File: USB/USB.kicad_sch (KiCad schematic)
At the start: 33 parts, among them J1 MISC1, U1 TLV61222

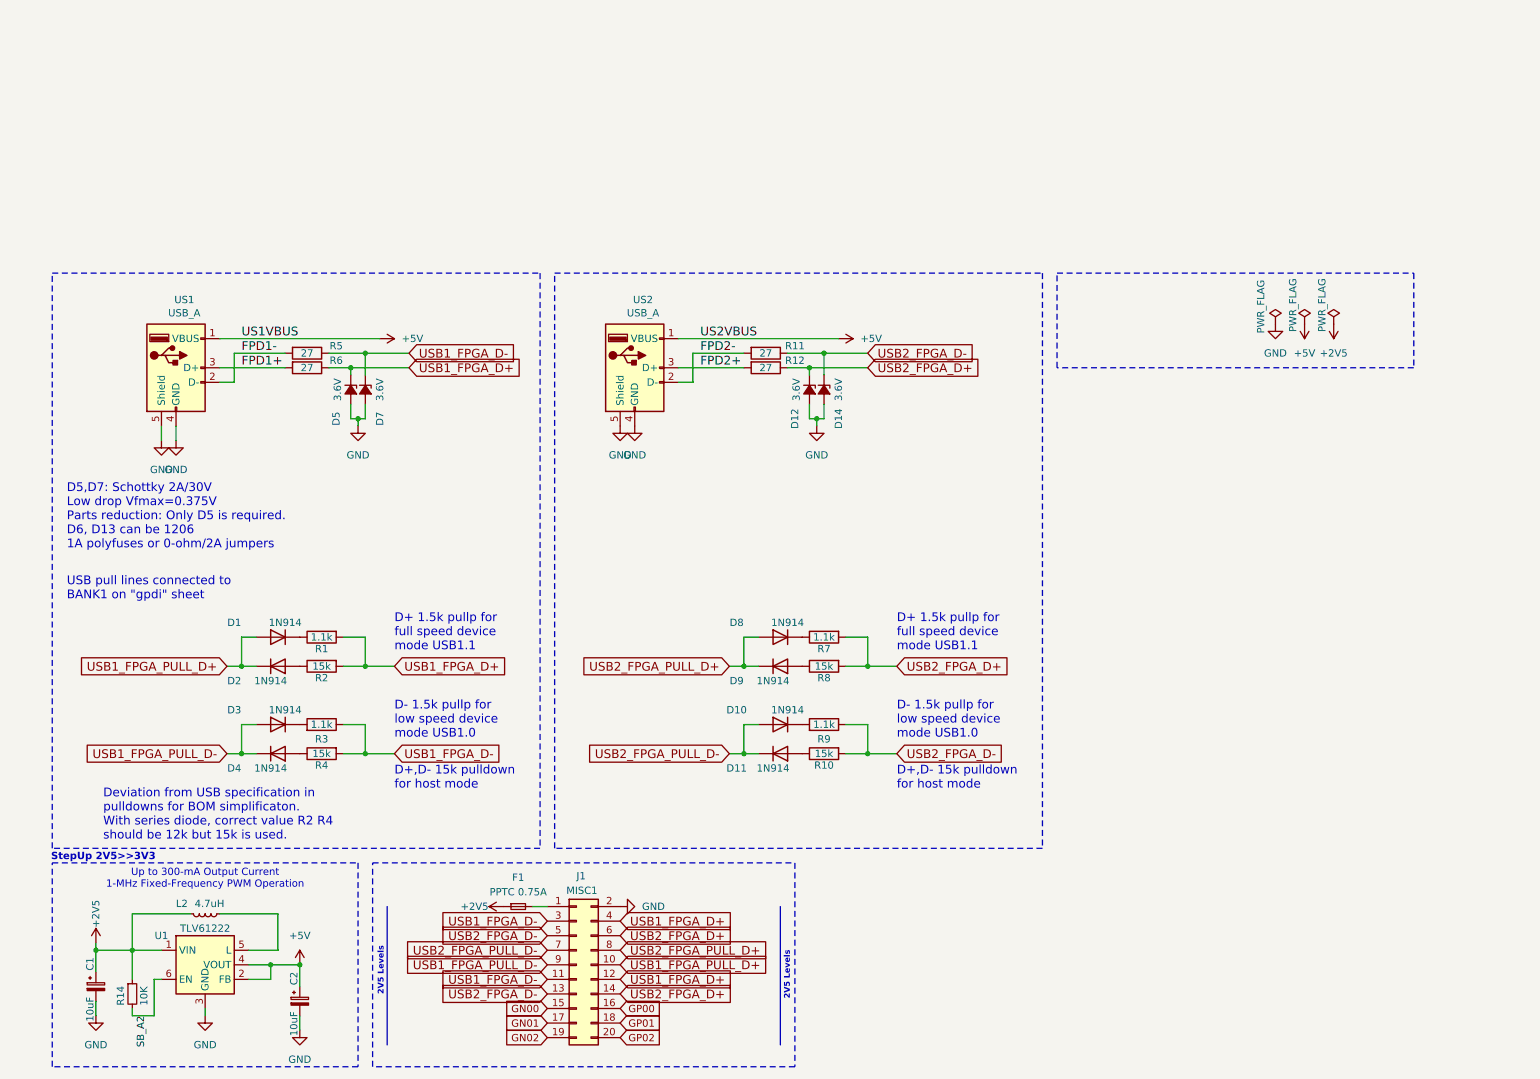
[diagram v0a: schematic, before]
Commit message: Updating USB
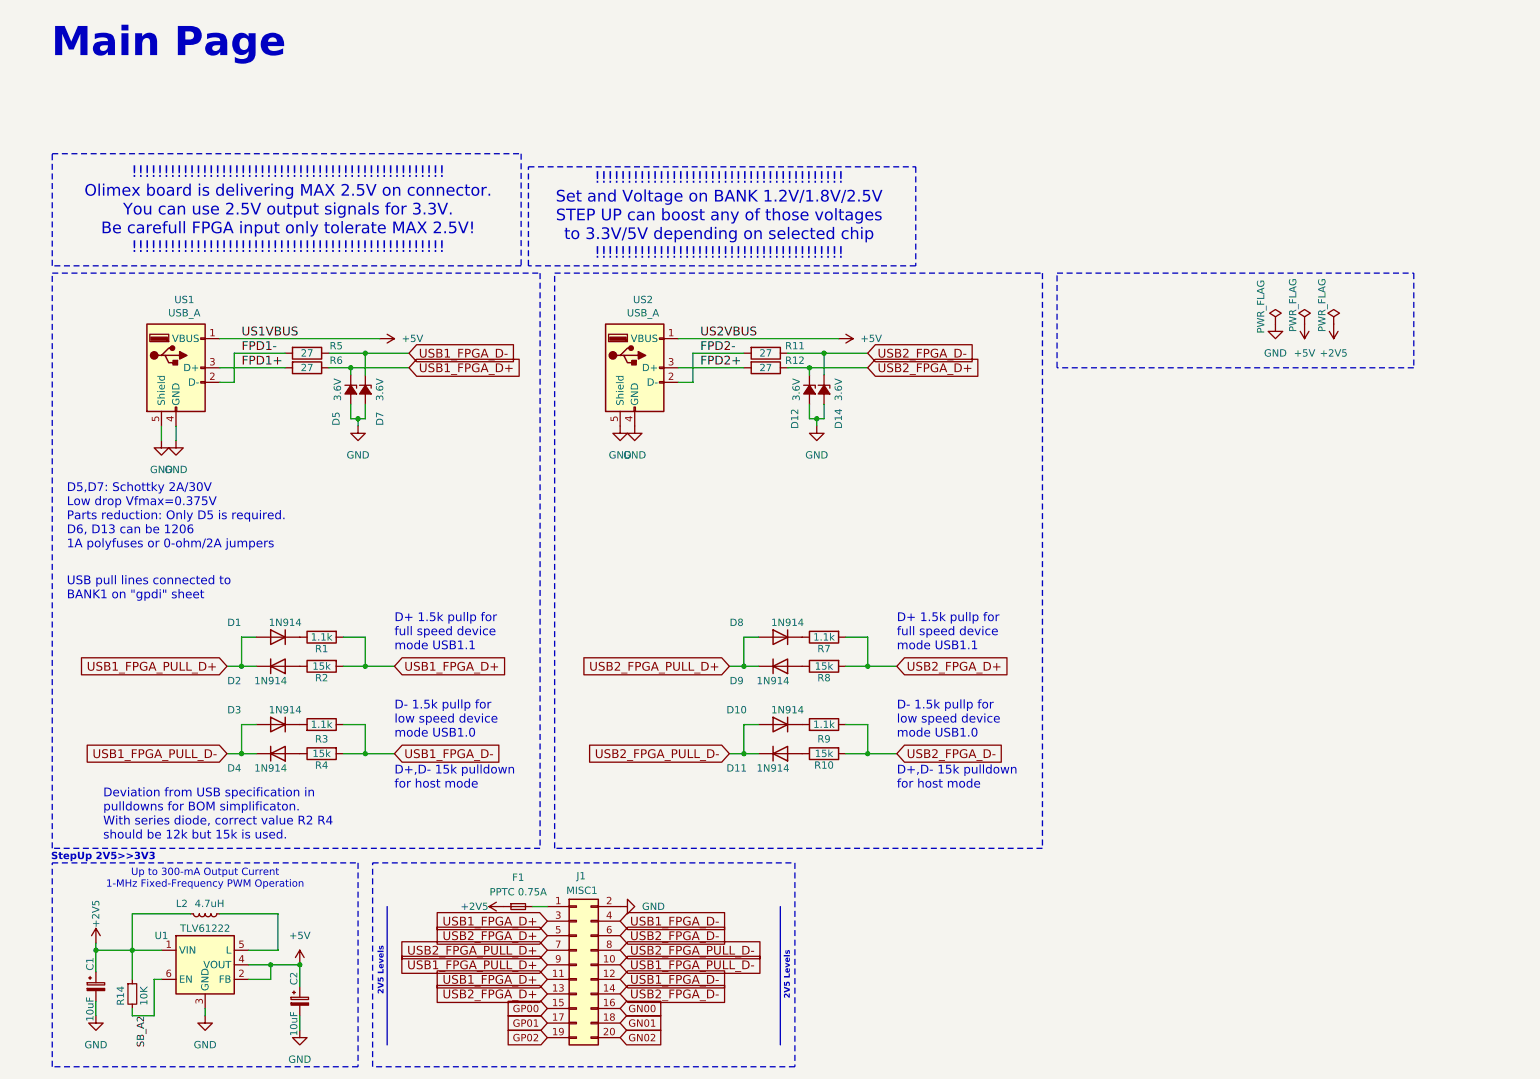
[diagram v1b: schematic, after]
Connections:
- net GN00: now also J1.16 (Pin_16); no longer J1.15 (Pin_15)
- net GN01: now also J1.18 (Pin_18); no longer J1.17 (Pin_17)
- net GN02: now also J1.20 (Pin_20); no longer J1.19 (Pin_19)
- net GP00: now also J1.15 (Pin_15); no longer J1.16 (Pin_16)
- net GP01: now also J1.17 (Pin_17); no longer J1.18 (Pin_18)
- net GP02: now also J1.19 (Pin_19); no longer J1.20 (Pin_20)
- net USB1_FPGA_D+: now also J1.11 (Pin_11), J1.3 (Pin_3); no longer J1.12 (Pin_12), J1.4 (Pin_4)
- net USB1_FPGA_D-: now also J1.12 (Pin_12), J1.4 (Pin_4); no longer J1.11 (Pin_11), J1.3 (Pin_3)
- net USB1_FPGA_PULL_D+: now also J1.9 (Pin_9); no longer J1.10 (Pin_10)
- net USB1_FPGA_PULL_D-: now also J1.10 (Pin_10); no longer J1.9 (Pin_9)
- net USB2_FPGA_D+: now also J1.13 (Pin_13), J1.5 (Pin_5); no longer J1.14 (Pin_14), J1.6 (Pin_6)
- net USB2_FPGA_D-: now also J1.14 (Pin_14), J1.6 (Pin_6); no longer J1.13 (Pin_13), J1.5 (Pin_5)
- net USB2_FPGA_PULL_D+: now also J1.7 (Pin_7); no longer J1.8 (Pin_8)
- net USB2_FPGA_PULL_D-: now also J1.8 (Pin_8); no longer J1.7 (Pin_7)
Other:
- note added: "!!!!!!!!!!!!!!!!!!!!!!!!!!!!!!!!!!!!!!! Set and Voltage on BANK 1.2V/1.8V/2.5V STEP UP can boost any of those voltages to 3.3V/5V depending on selected chip !!!!!!!!!!!!!!!!!!!!!!!!!!!!!!!!!!!!!!!"
- note added: "!!!!!!!!!!!!!!!!!!!!!!!!!!!!!!!!!!!!!!!!!!!!!!!!! Olimex board is delivering MAX 2.5V on connector. You can use 2.5V output signals for 3.3V. Be carefull FPGA input only tolerate MAX 2.5V! !!!!!!!!!!!!!!!!!!!!!!!!!!!!!!!!!!!!!!!!!!!!!!!!!"
- note added: "Main Page"

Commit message: Adding voltage level converter for USB
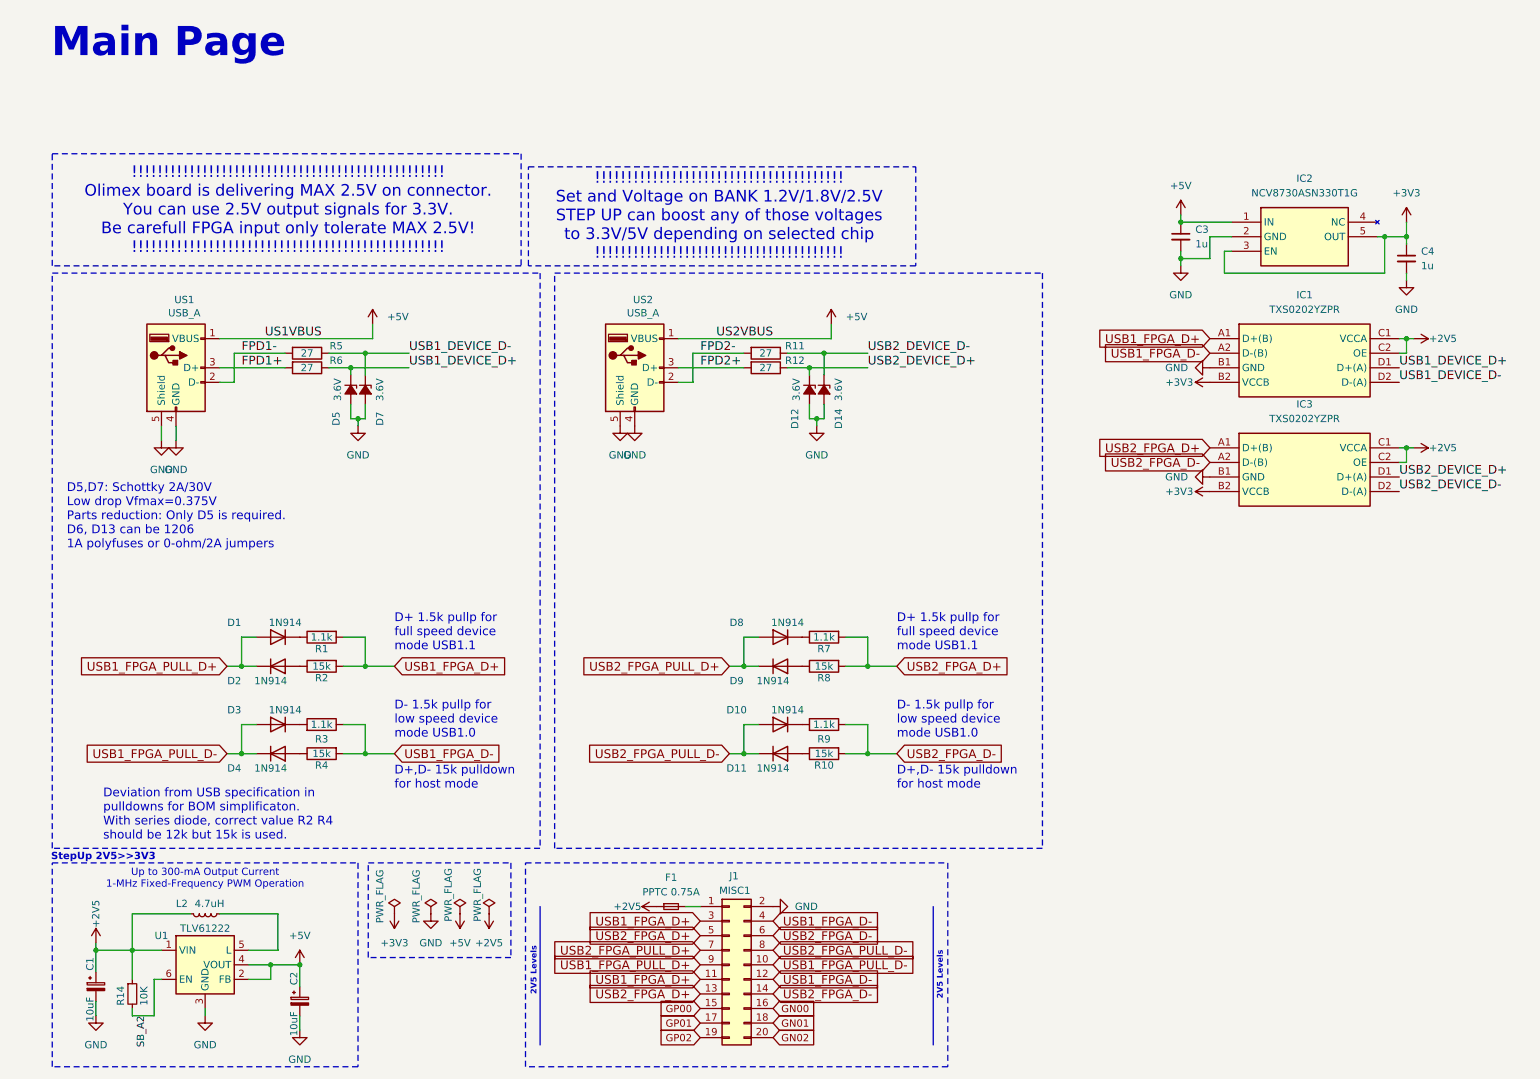
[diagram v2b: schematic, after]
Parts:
- added C3, C4: 1u, Capacitor_SMD:C_0603_1608Metric, symbol Device:C_Small
- added IC1, IC3: TXS0202YZPR, TXS0202YZPR:BGA8C50P2X4_89X189X50, symbol TXS0202YZPR:TXS0202YZPR
- added IC2: NCV8730ASN330T1G, NCV8730ASN330T1G:SOT95P275X110-5N, symbol NCV8730ASN330T1G:NCV8730ASN330T1G
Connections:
- net +2V5: now also IC1.C1 (VCCA), IC1.C2 (OE), IC3.C1 (VCCA), IC3.C2 (OE)
- net +5V: now also C3.1, IC2.1 (IN)
- net GND: now also C3.2, C4.2, IC1.B1 (GND), IC2.2 (GND), IC3.B1 (GND)
- net USB1_FPGA_D+: now also IC1.A1 (D+(B)); no longer D5.1 (K), R6.1
- net USB1_FPGA_D-: now also IC1.A2 (D-(B)); no longer D7.1 (K), R5.1
- net USB2_FPGA_D+: now also IC3.A1 (D+(B)); no longer D12.1 (K), R12.1
- net USB2_FPGA_D-: now also IC3.A2 (D-(B)); no longer D14.1 (K), R11.1
- new net +3V3: C4.1, IC1.B2 (VCCB), IC2.3 (EN), IC2.5 (OUT), IC3.B2 (VCCB)
- new net USB1_DEVICE_D+: D5.1 (K), IC1.D1 (D+(A)), R6.1
- new net USB1_DEVICE_D-: D7.1 (K), IC1.D2 (D-(A)), R5.1
- new net USB2_DEVICE_D+: D12.1 (K), IC3.D1 (D+(A)), R12.1
- new net USB2_DEVICE_D-: D14.1 (K), IC3.D2 (D-(A)), R11.1
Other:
- note removed: "USB pull lines connected to BANK1 on "gpdi" sheet"
- moved on the sheet: F1, J1

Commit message: Moving schematics to v9 adding more details
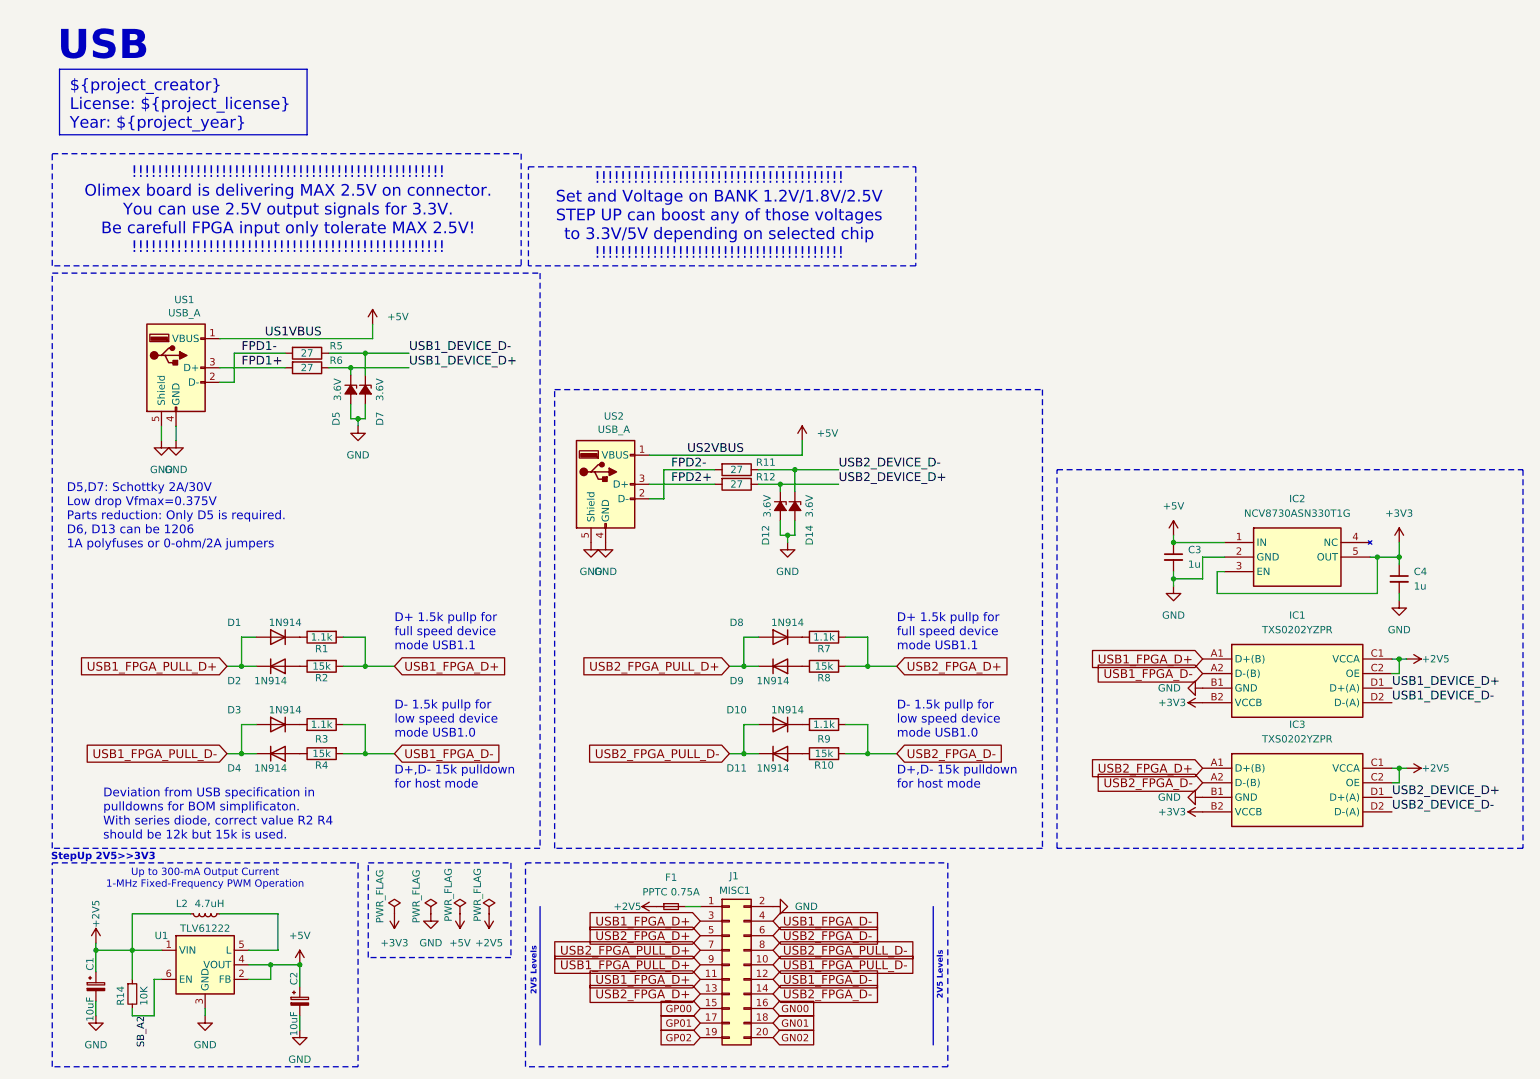
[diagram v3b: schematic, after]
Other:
- note added: "${project_creator} License: ${project_license} Year: ${project_year}"
- note added: "USB"
- note removed: "Main Page"
- company: (none) -> ${project_creator}
- title: (none) -> ${project_name} ${project_version}
- moved on the sheet: C3, C4, D12, D14, IC1, IC2, IC3, R11, R12, US2

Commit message: Fix #7
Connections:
- net +2V5: now also IC1.B2 (VCCB), IC3.B2 (VCCB); no longer IC1.C1 (VCCA), IC1.C2 (OE), IC3.C1 (VCCA), IC3.C2 (OE)
- net +3V3: now also IC1.C1 (VCCA), IC1.C2 (OE), IC3.C1 (VCCA), IC3.C2 (OE); no longer IC1.B2 (VCCB), IC3.B2 (VCCB)
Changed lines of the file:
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@@
 			"AFcASgBIAE8ARwBVAFQARwBXAFYATgBzAGsAbwB0AHkAegArAEwAYgBlAGIAMQBHAGkAOABpAEgA"
 			"UwBTAHoAZABOADEATwBnAEMAZwBSAEkATwBVAFUAZwBEAEkARABIAGYAUgAxAHUAdgB5AGEAWQBl"
-			"AHIAZgBpAG8AZQBVAFkATQBxAGsARwBSAHIARwBEADYALwA5ADUAQQAvADQATQBYAA=="
+			"AHIAZgBpAG8AZQBVAFkATQBxAGsARwBSAHIARwBEADYALwA5ADUAQQAvADQATQBYADIAagB5AFAA"
+			"QQBTAFEANQBEAEkARgBDAEEAeQAyAEsAQQB6AGsATQBqAGoAcABvAGgASQBCAEIANQAzADAAMQBQ"
+			"ADUAMwB5AFAAUgBBAHgARgAyAEgAZgB0AC8AVwBJAHAAbQA2AGQARgA5AHIAdgA4AHUAZgAxAC8A"
+			"KwBmAHUAcgAxAE0AbwBIAEgAcABTADEAaQBXAEcANABDAHkATQBLAHkATQBYAGcARwBLAE8AVwB3"
+			"AEsAcQB1AG8AVABEAEgAbABNAEQAagA0AHMAYgBvAFgAKwAxAHgAegBiADUAbQBvAEwAOQBIAHMA"
+			"MwBxAEwAdgA2AGsAMwAvAFgAZgA0AGEAQQBpAEEAcwBLAFIAbQBOAHYAQwA2AEsAcwBFAHkANAA5"
+			"AGwASABhAHgAcwBpADgAMABmAHUARQBKAFEASgB2AGQAUABvAFAAUwArAGIAbABKAGQASABrAFgA"
+			"dQB6ADcANwBQADUAZQBOADgAVwBoAEIAbwBJAHcATgBjAFoAZAArAEIAQQA4AHcAdgBxADkAQgBX"
+			"AGgAaAB4AEgAUgBMAGgAdgBaAGsASQBpAHcANABhAHIATQBrADgAYwB3AGIAdwBuAHMAbgBRAHkA"
+			"agBPAGIAbwBWAGIATwBnAGgAQgByAEYAcQBiAC8AcgB4AEIAbwBoAFoAUwBuADIAUQB4AEoANQB1"
+			"AGIAagBaAG8ASwBMADAAdABaAEMAaAB4AHEAbwBlAFkAcwBuAEsAegBKAGsAegAyAFcAcgBLAEYA"
+			"ZgBRAG4AWQB5AHUAMgB6AGwAbwBzAEsAeAA2AE4ANgB0AHAANABZAGQARQBBADgAWQBZAEEAZQBJ"
+			"ADAAWQBOAFEAUgBxAHcAaABJAHgAQgBLAHIAMwBuAEMATQAxAE0AbwBwAFQAaAAwADYAQgBBADgA"
+			"SABnACsAeQBzADcATQAxAEEASQBqAFIAeABqAFcAaAA1AGoAVQBBAEMAKwBMADkAUABpAEUARQAx"
+			"AGQAVQBCAHoATgBLAHgAaABhADYAYgB2AGgAeQBEAHoAaABxAHMAWgBqAG4AVABtAHgAagBjAFkA"
+			"YQBMAFcAUwBrAHAANAAwAGYAdgAwAEIANgBwAHcAMwBVADIAeABxAGUAeQBOAG0ARQBsADIAbQBF"
+			"AFAAOAB6ADQAawB6AGgAeABwADIAUgBtAEkAQwBYAHYAYgBvADEAaABNAEEARABOAGwAUgBQAEwA"
+			"agBJAHcAaAAzAGQAYgBqAGMAYQBHAGgAcgBVAHQAUABSAHAAYQBXAGsAcQA0ADQAYwBYAFYAVwBl"
+			"AC8ASAB6AGwAeQBCAEoAbQBaAG0AZgBCADQAUABHAHIAVwByAFoAWgBvAGkAdABCAA=="
 		)
 	)
@@
 		(lib_name "+5V_1")
 		(lib_id "power:+5V")
-		(at 217.17 132.08 90)
+		(at 252.73 124.46 270)
 		(unit 1)
 		(exclude_from_sim no)
@@
 		(dnp no)
 		(property "Reference" "#PWR013"
-			(at 220.98 132.08 0)
+			(at 248.92 124.46 0)
 			(effects
 				(font
@@
 		)
 		(property "Value" "+3V3"
-			(at 211.836 132.08 90)
+			(at 258.064 124.46 90)
 			(effects
 				(font
@@
 		)
 		(property "Footprint" ""
-			(at 217.17 132.08 0)
+			(at 252.73 124.46 0)
 			(effects
 				(font
@@
 		)
 		(property "Datasheet" ""
-			(at 217.17 132.08 0)
+			(at 252.73 124.46 0)
 			(effects
 				(font
@@
 		)
 		(property "Description" "Power symbol creates a global label with name \"+5V\""
-			(at 217.17 132.08 0)
+			(at 252.73 124.46 0)
 			(effects
 				(font
@@
 		(lib_name "+5V_1")
 		(lib_id "power:+5V")
-		(at 252.73 143.51 270)
+		(at 217.17 151.13 90)
 		(unit 1)
 		(exclude_from_sim no)
@@
 		(dnp no)
 		(property "Reference" "#PWR027"
-			(at 248.92 143.51 0)
+			(at 220.98 151.13 0)
 			(effects
 				(font
@@
 		)
 		(property "Value" "+2V5"
-			(at 257.81 143.51 90)
+			(at 212.09 151.13 90)
 			(effects
 				(font
@@
 		)
 		(property "Footprint" ""
-			(at 252.73 143.51 0)
+			(at 217.17 151.13 0)
 			(effects
 				(font
@@
 		)
 		(property "Datasheet" ""
-			(at 252.73 143.51 0)
+			(at 217.17 151.13 0)
 			(effects
 				(font
@@
 		)
 		(property "Description" "Power symbol creates a global label with name \"+5V\""
-			(at 252.73 143.51 0)
+			(at 217.17 151.13 0)
 			(effects
 				(font
@@
 		(lib_name "+5V_1")
 		(lib_id "power:+5V")
-		(at 252.73 124.46 270)
+		(at 217.17 132.08 90)
 		(unit 1)
 		(exclude_from_sim no)
@@
 		(dnp no)
 		(property "Reference" "#PWR016"
-			(at 248.92 124.46 0)
+			(at 220.98 132.08 0)
 			(effects
 				(font
@@
 		)
 		(property "Value" "+2V5"
-			(at 257.81 124.46 90)
+			(at 212.09 132.08 90)
 			(effects
 				(font
@@
 		)
 		(property "Footprint" ""
-			(at 252.73 124.46 0)
+			(at 217.17 132.08 0)
 			(effects
 				(font
@@
 		)
 		(property "Datasheet" ""
-			(at 252.73 124.46 0)
+			(at 217.17 132.08 0)
 			(effects
 				(font
@@
 		)
 		(property "Description" "Power symbol creates a global label with name \"+5V\""
-			(at 252.73 124.46 0)
+			(at 217.17 132.08 0)
 			(effects
 				(font
@@
 		(lib_name "+5V_1")
 		(lib_id "power:+5V")
-		(at 217.17 151.13 90)
+		(at 252.73 143.51 270)
 		(unit 1)
 		(exclude_from_sim no)
@@
 		(dnp no)
 		(property "Reference" "#PWR029"
-			(at 220.98 151.13 0)
+			(at 248.92 143.51 0)
 			(effects
 				(font
@@
 		)
 		(property "Value" "+3V3"
-			(at 211.836 151.13 90)
+			(at 258.064 143.51 90)
 			(effects
 				(font
@@
 		)
 		(property "Footprint" ""
-			(at 217.17 151.13 0)
+			(at 252.73 143.51 0)
 			(effects
 				(font
@@
 		)
 		(property "Datasheet" ""
-			(at 217.17 151.13 0)
+			(at 252.73 143.51 0)
 			(effects
 				(font
@@
 		)
 		(property "Description" "Power symbol creates a global label with name \"+5V\""
-			(at 217.17 151.13 0)
+			(at 252.73 143.51 0)
 			(effects
 				(font
